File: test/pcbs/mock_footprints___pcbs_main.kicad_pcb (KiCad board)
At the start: 2 copper layers, 39 x 19 mm, 9 parts

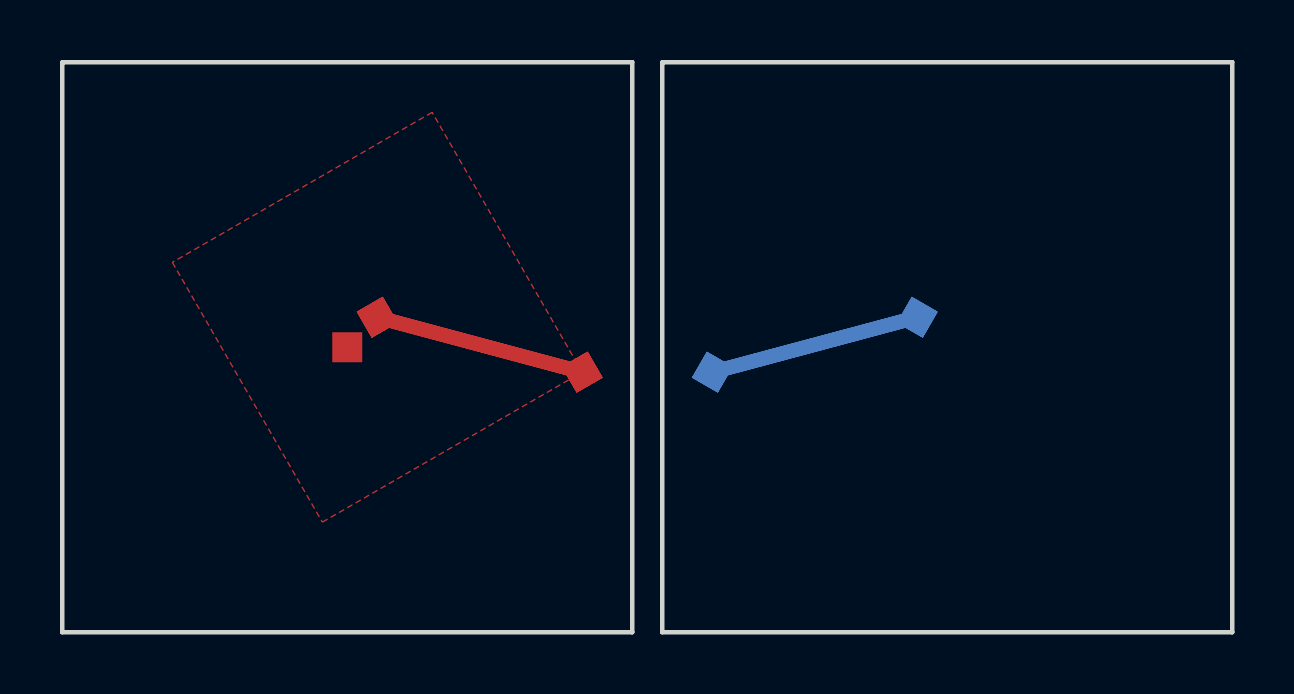
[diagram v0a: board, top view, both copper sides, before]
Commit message: Filter/mirror bugfix
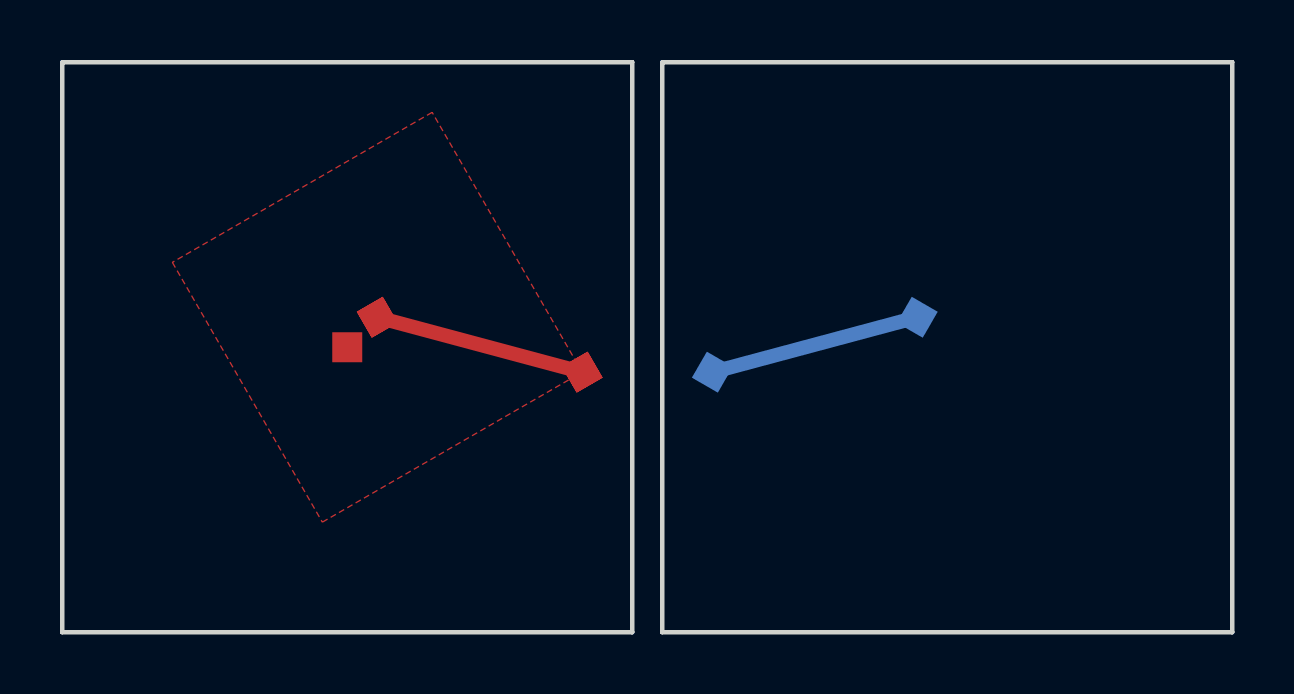
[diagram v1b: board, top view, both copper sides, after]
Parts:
- removed the ? at (1.00, -1.00) (x2)
- removed the ? at (19.0, -1.00) (x2)
- removed the ? at (0.00, 0.00) (x2)
- added ?: , trace_test, F.Cu at (1.00, -1.00)
- added ?: , trace_test, B.Cu at (19.0, -1.00)
- added ? (x2): , anchor_test, F.Cu at (0.00, 0.00)
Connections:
- net T6_3 renamed T4_3
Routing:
- net P1: track 28.3 -> 14.1 mm
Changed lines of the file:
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@@
             (net 0 "")
 (net 1 "P1")
-(net 2 "T6_1")
-(net 3 "T6_2")
-(net 4 "T6_3")
+(net 2 "T4_1")
+(net 3 "T4_2")
+(net 4 "T4_3")
   (net_class Default "This is the default net class."
     (clearance 0.2)
@@
     (add_net "")
 (add_net "P1")
-(add_net "T6_1")
-(add_net "T6_2")
-(add_net "T6_3")
+(add_net "T4_1")
+(add_net "T4_2")
+(add_net "T4_3")
   )
                 (module trace_test (layer F.Cu)
@@
                 )
                 (segment (start 19 -1) (end 12.169872999999999 0.8301270000000001) (width 0.475) (layer B.Cu) (net 1))
-                (module trace_test (layer B.Cu)
-                    (at 19 -1 -30)
-                    (pad 1 smd rect (at 0 0 -30) (size 1 1) (layers B.Cu B.Paste B.Mask)
-                        (net 1 "P1") (solder_mask_margin 0.2))
-                    (pad 2 smd rect (at -5 5 -30) (size 1 1) (layers B.Cu B.Paste B.Mask)
-                        (net 1 "P1") (solder_mask_margin 0.2))
-                )
-                (segment (start 19 -1) (end 12.169872999999999 0.8301270000000001) (width 0.475) (layer B.Cu) (net 1))
-                (module trace_test (layer F.Cu)
-                    (at 1 -1 30)
-                    (pad 1 smd rect (at 0 0 30) (size 1 1) (layers F.Cu F.Paste F.Mask)
-                        (net 1 "P1") (solder_mask_margin 0.2))
-                    (pad 2 smd rect (at 5 5 30) (size 1 1) (layers F.Cu F.Paste F.Mask)
-                        (net 1 "P1") (solder_mask_margin 0.2))
-                )
-                (segment (start 1 -1) (end 7.830127 0.8301270000000001) (width 0.475) (layer F.Cu) (net 1))
                 (module zone_test (layer F.Cu)
                     (at 1 -1 30)
@@
                     (at 0 0 0)
                     (pad 1 smd rect (at 0 0 0) (size 1 1) (layers F.Cu F.Paste F.Mask)
-                        (net 2 "T6_1") (solder_mask_margin 0.2))
+                        (net 2 "T4_1") (solder_mask_margin 0.2))
                     (pad 1 smd rect (at 0 0 0) (size 1 1) (layers F.Cu F.Paste F.Mask)
-                        (net 3 "T6_2") (solder_mask_margin 0.2))
+                        (net 3 "T4_2") (solder_mask_margin 0.2))
                     (pad 1 smd rect (at 0 0 0) (size 1 1) (layers F.Cu F.Paste F.Mask)
-                        (net 4 "T6_3") (solder_mask_margin 0.2))
+                        (net 4 "T4_3") (solder_mask_margin 0.2))
                 )
                 (module anchor_test (layer F.Cu)

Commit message: Templating bugfix (#86)
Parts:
- removed the ? at (0.00, 0.00) (x3)
- added ? (x2): , anchor_test, F.Cu at (0.00, 0.00)
- added ? (x2): , arrobj_test, F.Cu at (0.00, 0.00)
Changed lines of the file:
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@@
 (fp_line (start 5 5) (end 7 7) (layer Dwgs.User) (width 0.05))
+                )
+                (module arrobj_test (layer F.Cu)
+                    (at 0 0 0)
+                    (fp_line (start 5 5) (end 6 6) (layer Dwgs.User) (width 0.05))
+(fp_line (start 5 5) (end 7 5) (layer Dwgs.User) (width 0.05))
                 )
             (gr_line (start -9.5 9.5) (end 9.5 9.5) (angle 90) (layer Edge.Cuts) (width 0.15))

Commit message: Injectable PCB templates
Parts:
- removed the ? at (0.00, 0.00) (x4)
- added ? (x2): , anchor_test, F.Cu at (0.00, 0.00)
- added ? (x2): , arrobj_test, F.Cu at (0.00, 0.00)
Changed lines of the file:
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@@
       (outputdirectory ""))
   )
-            (net 0 "")
+  (net 0 "")
 (net 1 "P1")
 (net 2 "T4_1")
@@
 (fp_line (start 5 5) (end 7 5) (layer Dwgs.User) (width 0.05))
                 )
-            (gr_line (start -9.5 9.5) (end 9.5 9.5) (angle 90) (layer Edge.Cuts) (width 0.15))
+  (gr_line (start -9.5 9.5) (end 9.5 9.5) (angle 90) (layer Edge.Cuts) (width 0.15))
 (gr_line (start 9.5 9.5) (end 9.5 -9.5) (angle 90) (layer Edge.Cuts) (width 0.15))
 (gr_line (start 9.5 -9.5) (end -9.5 -9.5) (angle 90) (layer Edge.Cuts) (width 0.15))

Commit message: Add missing quotes for PCB metadata (#125)
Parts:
- removed the ? at (0.00, 0.00) (x4)
- added ? (x2): , anchor_test, F.Cu at (0.00, 0.00)
- added ? (x2): , arrobj_test, F.Cu at (0.00, 0.00)
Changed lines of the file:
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@@
   (page A3)
   (title_block
-    (title main)
-    (rev v1.0.0)
-    (company Unknown)
+    (title "main")
+    (rev "v1.0.0")
+    (company "Unknown")
   )
   (general
